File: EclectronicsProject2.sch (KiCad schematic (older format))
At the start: 65 parts, among them J7 Barrel_Jack, U11 TPS62290DRVR, U8 TPS62290DRVR

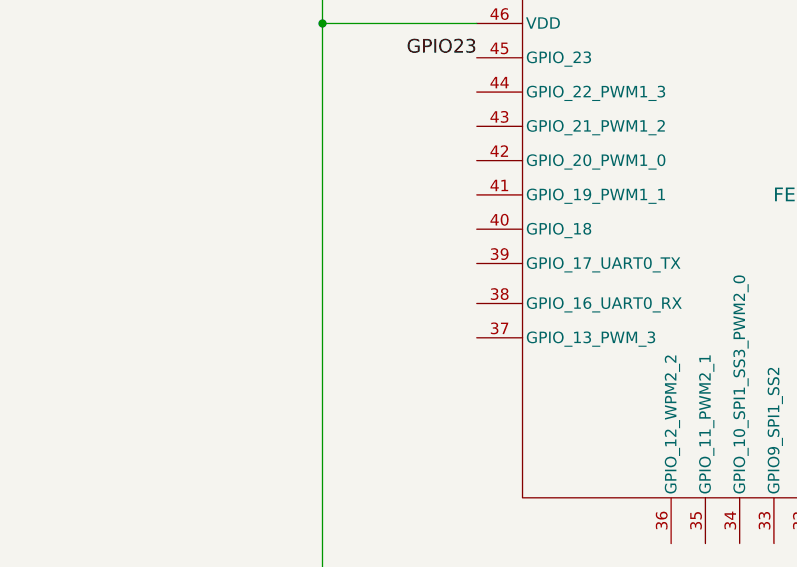
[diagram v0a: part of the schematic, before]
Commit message: adding GPIO UART connections
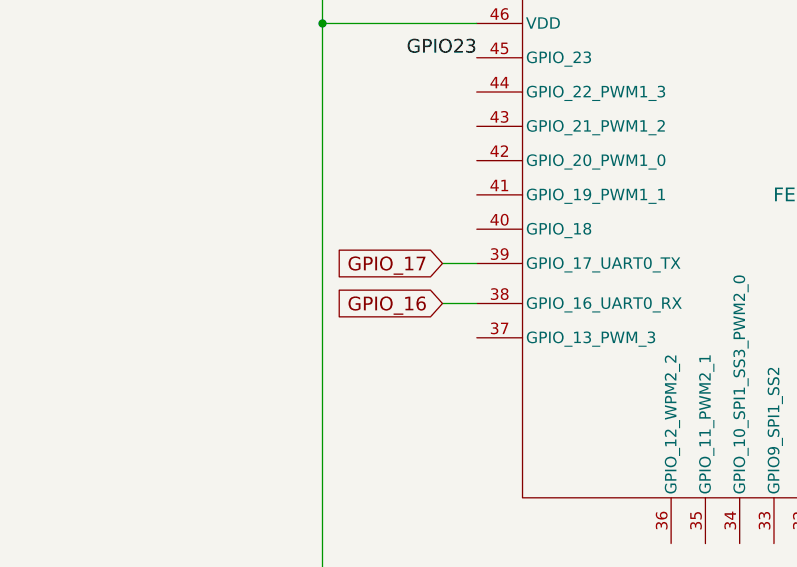
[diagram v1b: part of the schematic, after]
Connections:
- net GPIO_16: now reaches X?.38 (GPIO_16_UART0_RX)
- net GPIO_17: now reaches X?.39 (GPIO_17_UART0_TX)
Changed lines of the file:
@@
 Wire Wire Line
 	15125 5000 14975 5000
+Text GLabel 2275 3425 0    60   Input ~ 0
+GPIO_16
+Text GLabel 2275 3250 0    60   Input ~ 0
+GPIO_17
+Wire Wire Line
+	2275 3250 2425 3250
+Wire Wire Line
+	2275 3425 2425 3425
 $EndSCHEMATC

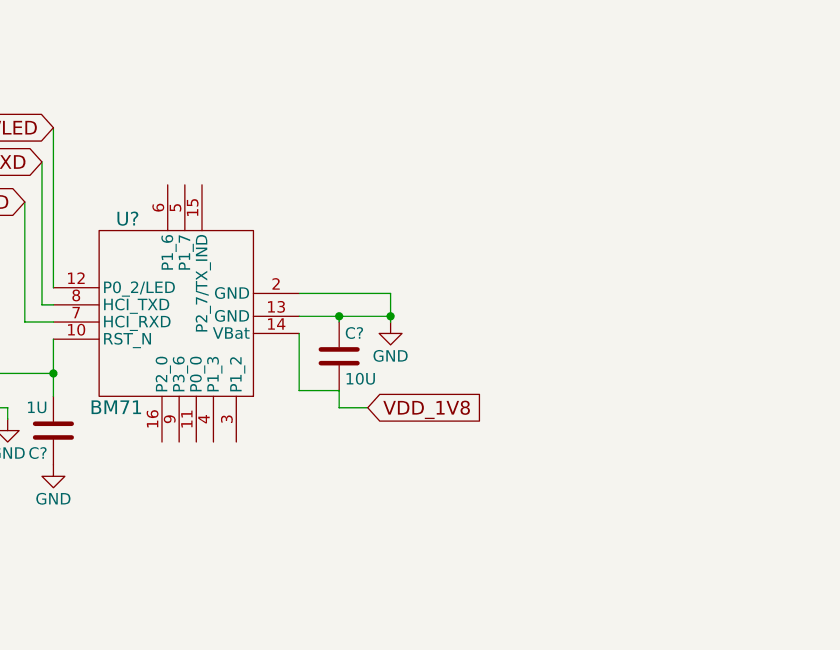
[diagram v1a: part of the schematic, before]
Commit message: added header pins to bm71 bluetooth
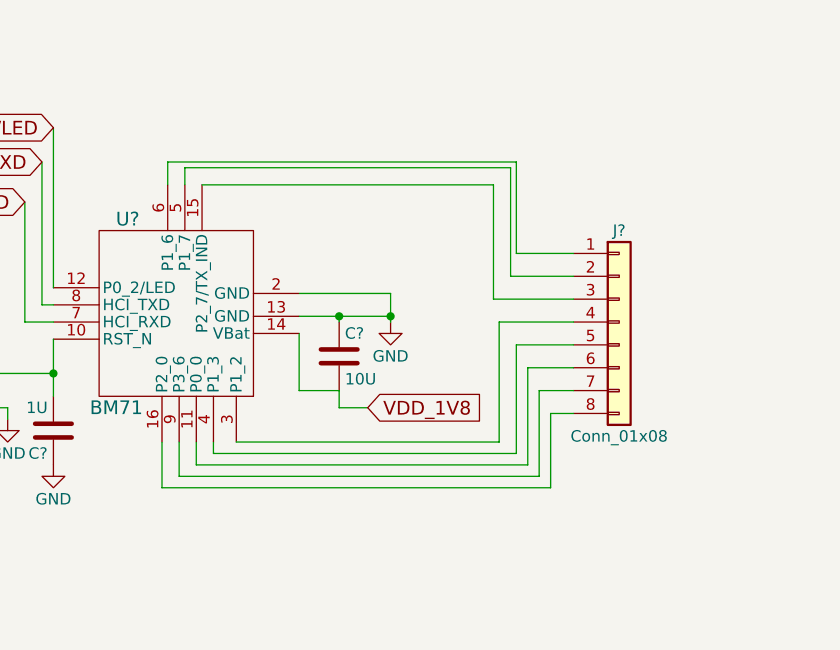
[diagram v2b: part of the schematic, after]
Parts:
- added J?: Conn_01x08, symbol Conn_01x08
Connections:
- net at U?.11 (P0_0): now also J?.6 (Pin_6)
- net at U?.15 (P2_7/TX_IND): now also J?.3 (Pin_3)
- net at U?.16 (P2_0): now also J?.8 (Pin_8)
- net at U?.3 (P1_2): now also J?.4 (Pin_4)
- net at U?.4 (P1_3): now also J?.5 (Pin_5)
- net at U?.5 (P1_7): now also J?.2 (Pin_2)
- net at U?.6 (P1_6): now also J?.1 (Pin_1)
- net at U?.9 (P3_6): now also J?.7 (Pin_7)
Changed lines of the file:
@@
 Wire Wire Line
 	2275 3425 2425 3425
+$Comp
+L Conn_01x08 J?
+U 1 1 59CE5643
+P 4625 6975
+F 0 "J?" H 4625 7375 50  0000 C CNN
+F 1 "Conn_01x08" H 4625 6475 50  0000 C CNN
+F 2 "" H 4625 6975 50  0001 C CNN
+F 3 "" H 4625 6975 50  0001 C CNN
+	1    4625 6975
+	1    0    0    -1
+$EndComp
+Wire Wire Line
+	2650 6375 2650 6275
+Wire Wire Line
+	2650 6275 4175 6275
+Wire Wire Line
+	4175 6275 4175 6675
+Wire Wire Line
+	4175 6675 4425 6675
+Wire Wire Line
+	2725 6375 2725 6300
+Wire Wire Line
+	2725 6300 4150 6300
+Wire Wire Line
+	4150 6300 4150 6775
+Wire Wire Line
+	4150 6775 4425 6775
+Wire Wire Line
+	2800 6375 4075 6375
+Wire Wire Line
+	4075 6375 4075 6875
+Wire Wire Line
+	4075 6875 4425 6875
+Wire Wire Line
+	2950 7500 4100 7500
+Wire Wire Line
+	4100 7500 4100 6975
+Wire Wire Line
+	4100 6975 4425 6975
+Wire Wire Line
+	2850 7500 2850 7550
+Wire Wire Line
+	2850 7550 4175 7550
+Wire Wire Line
+	4175 7550 4175 7075
+Wire Wire Line
+	4175 7075 4425 7075
+Wire Wire Line
+	4225 7175 4425 7175
+Wire Wire Line
+	4225 7175 4225 7600
+Wire Wire Line
+	4225 7600 2775 7600
+Wire Wire Line
+	2775 7600 2775 7500
+Wire Wire Line
+	4425 7275 4275 7275
+Wire Wire Line
+	4275 7275 4275 7650
+Wire Wire Line
+	4275 7650 2700 7650
+Wire Wire Line
+	2700 7650 2700 7500
+Wire Wire Line
+	4425 7375 4325 7375
+Wire Wire Line
+	4325 7375 4325 7700
+Wire Wire Line
+	4325 7700 2625 7700
+Wire Wire Line
+	2625 7700 2625 7500
 $EndSCHEMATC

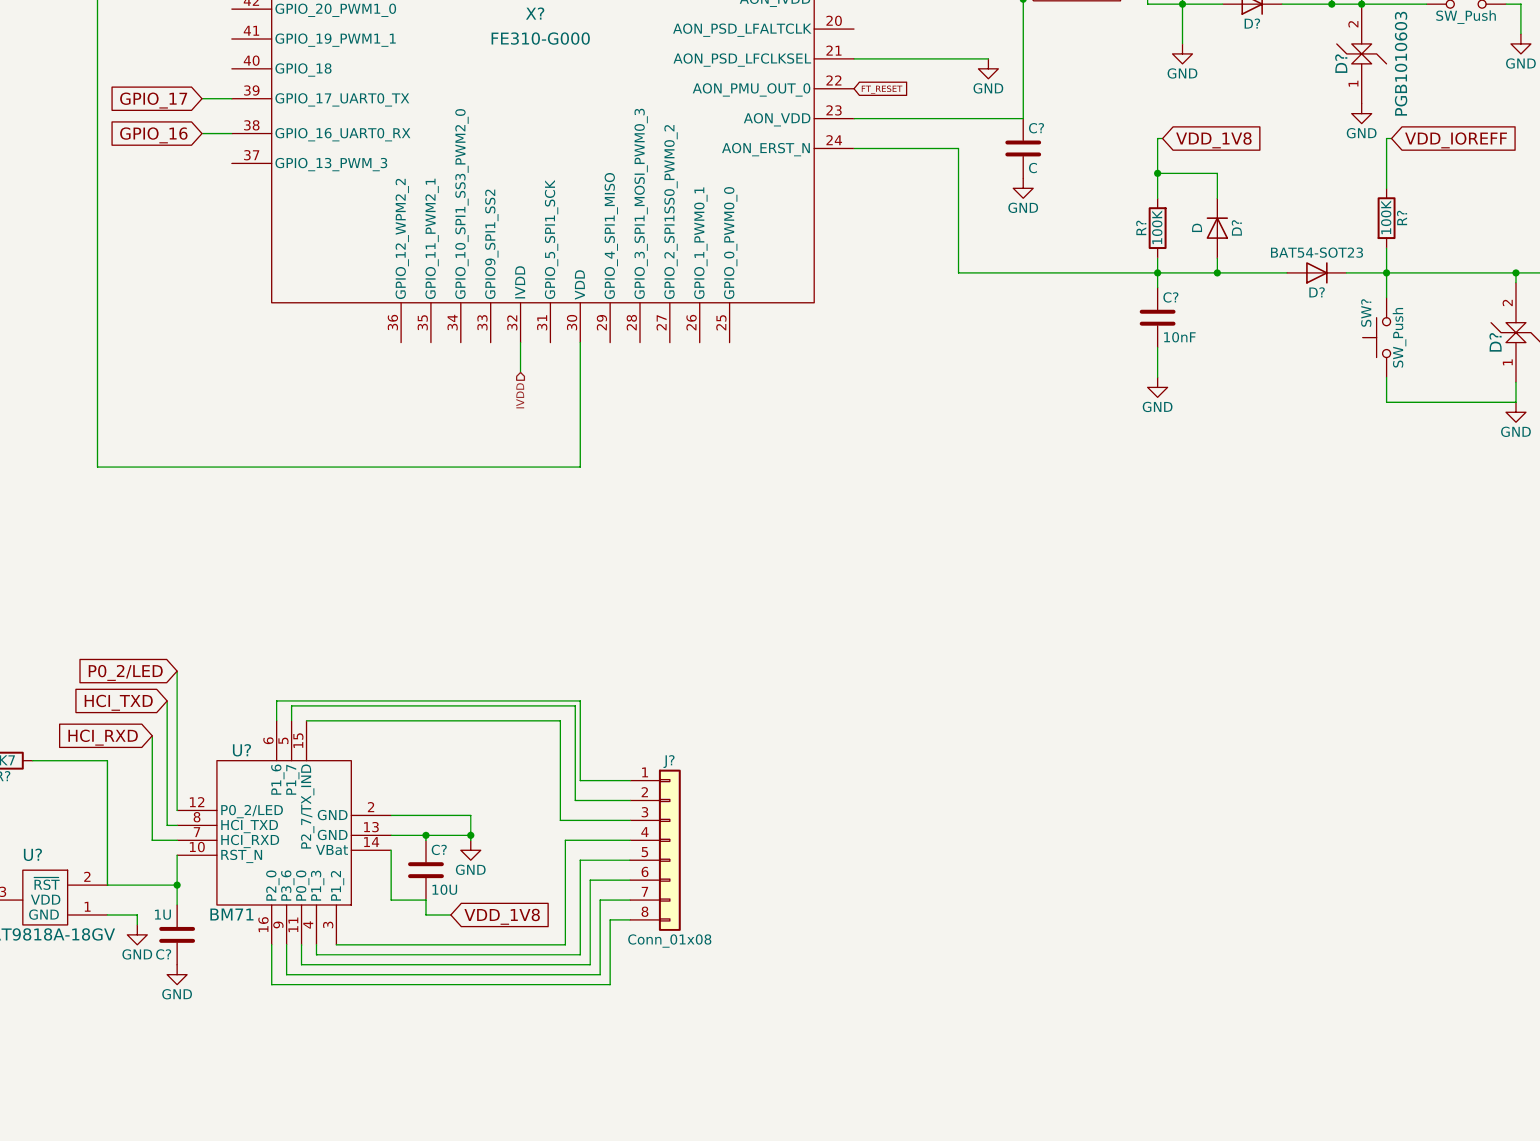
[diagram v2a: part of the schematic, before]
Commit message: attempted to add one of the TXS to header blocks, might be totally wrong
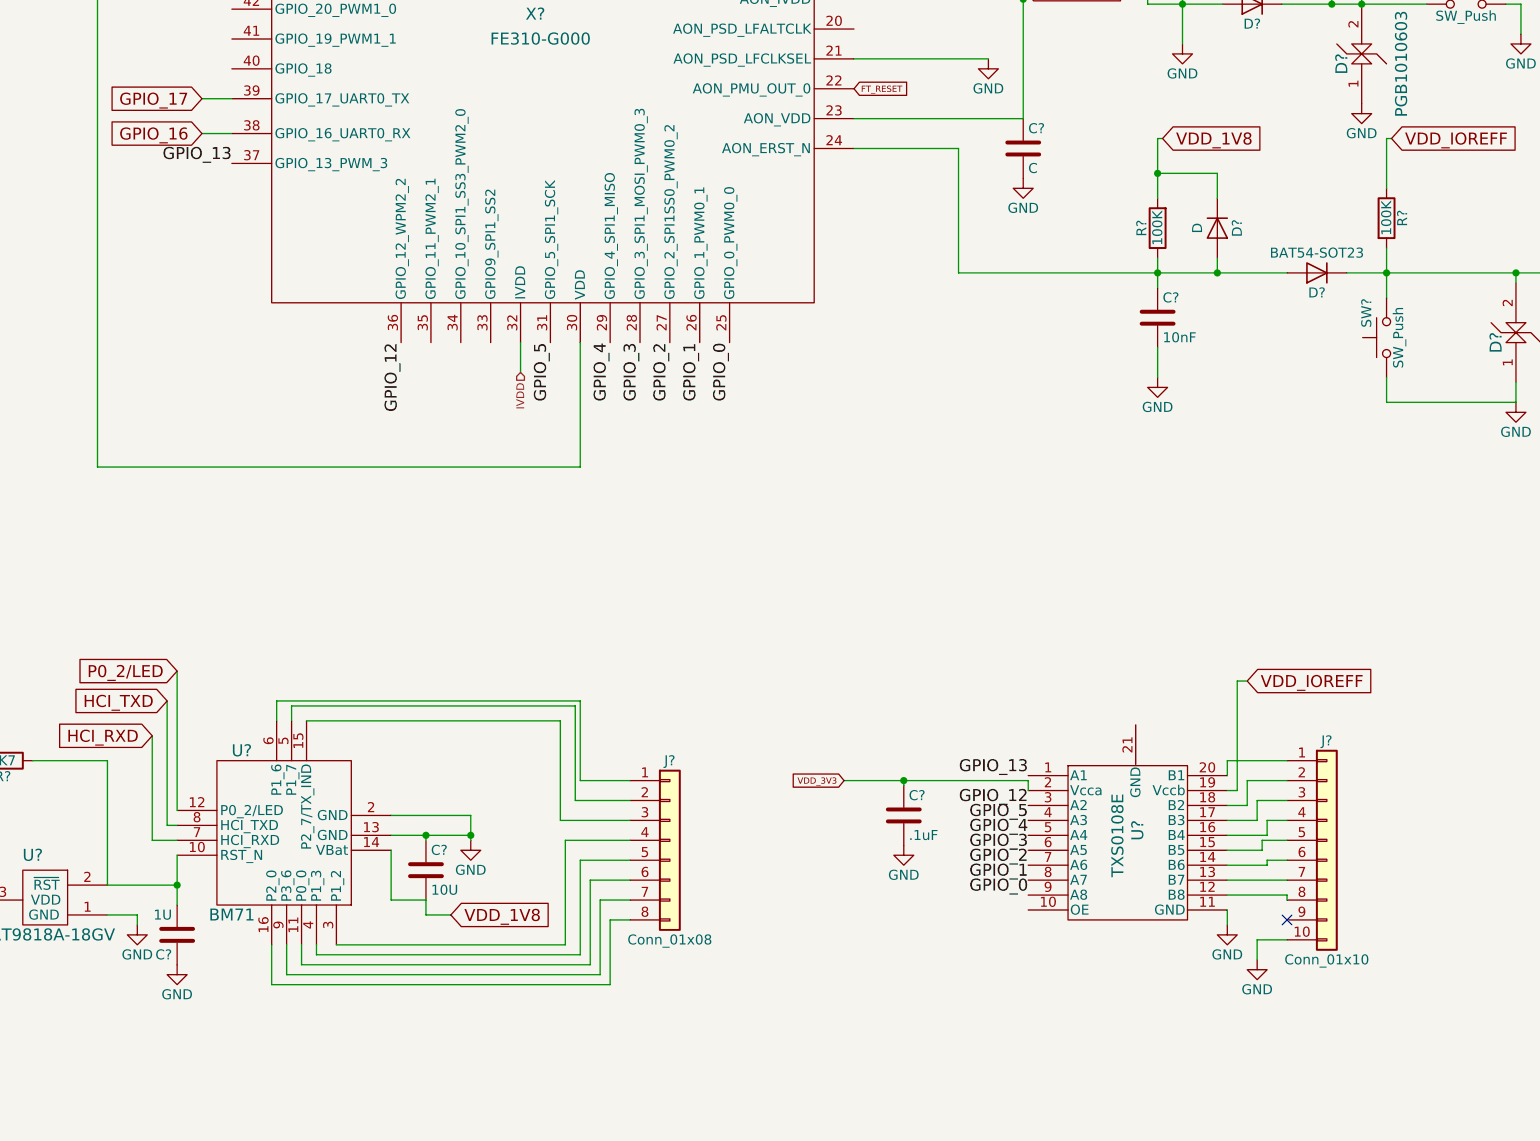
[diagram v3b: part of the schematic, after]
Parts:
- added C?: .1uF, symbol C
- added J?: Conn_01x10, symbol Conn_01x10
- added U?: TXS0108E, symbol TXS0108E
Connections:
- net GND: now also C?.2, J?.10 (Pin_10), U?.11 (GND)
- net VDD_3V3: now also C?.1, U?.2 (Vcca)
- net VDD_IOREFF: now also U?.19 (Vccb)
- net GPIO_0: now reaches X?.25 (GPIO_0_PWM0_0)
- net GPIO_0: now also U?.9 (A8)
- net GPIO_1: now reaches X?.26 (GPIO_1_PWM0_1)
- net GPIO_1: now also U?.8 (A7)
- net GPIO_2: now reaches X?.27 (GPIO_2_SPI1SS0_PWM0_2)
- net GPIO_2: now also U?.7 (A6)
- net GPIO_3: now reaches X?.28 (GPIO_3_SPI1_MOSI_PWM0_3)
- net GPIO_3: now also U?.6 (A5)
- net GPIO_4: now reaches X?.29 (GPIO_4_SPI1_MISO)
- net GPIO_4: now also U?.5 (A4)
- net GPIO_5: now reaches X?.31 (GPIO_5_SPI1_SCK)
- net GPIO_5: now also U?.4 (A3)
- net GPIO_12: now reaches X?.36 (GPIO_12_WPM2_2)
- net GPIO_12: now also U?.3 (A2)
- net GPIO_13: now reaches X?.37 (GPIO_13_PWM_3)
- net GPIO_13: now also U?.1 (A1)
- new net: J?.1 (Pin_1), U?.20 (B1)
- new net: J?.2 (Pin_2), U?.18 (B2)
- new net: J?.3 (Pin_3), U?.17 (B3)
- new net: J?.4 (Pin_4), U?.16 (B4)
- new net: J?.5 (Pin_5), U?.15 (B5)
- new net: J?.6 (Pin_6), U?.14 (B6)
- new net: J?.7 (Pin_7), U?.13 (B7)
- new net: J?.8 (Pin_8), U?.12 (B8)
- no-connect marks 1 -> 2

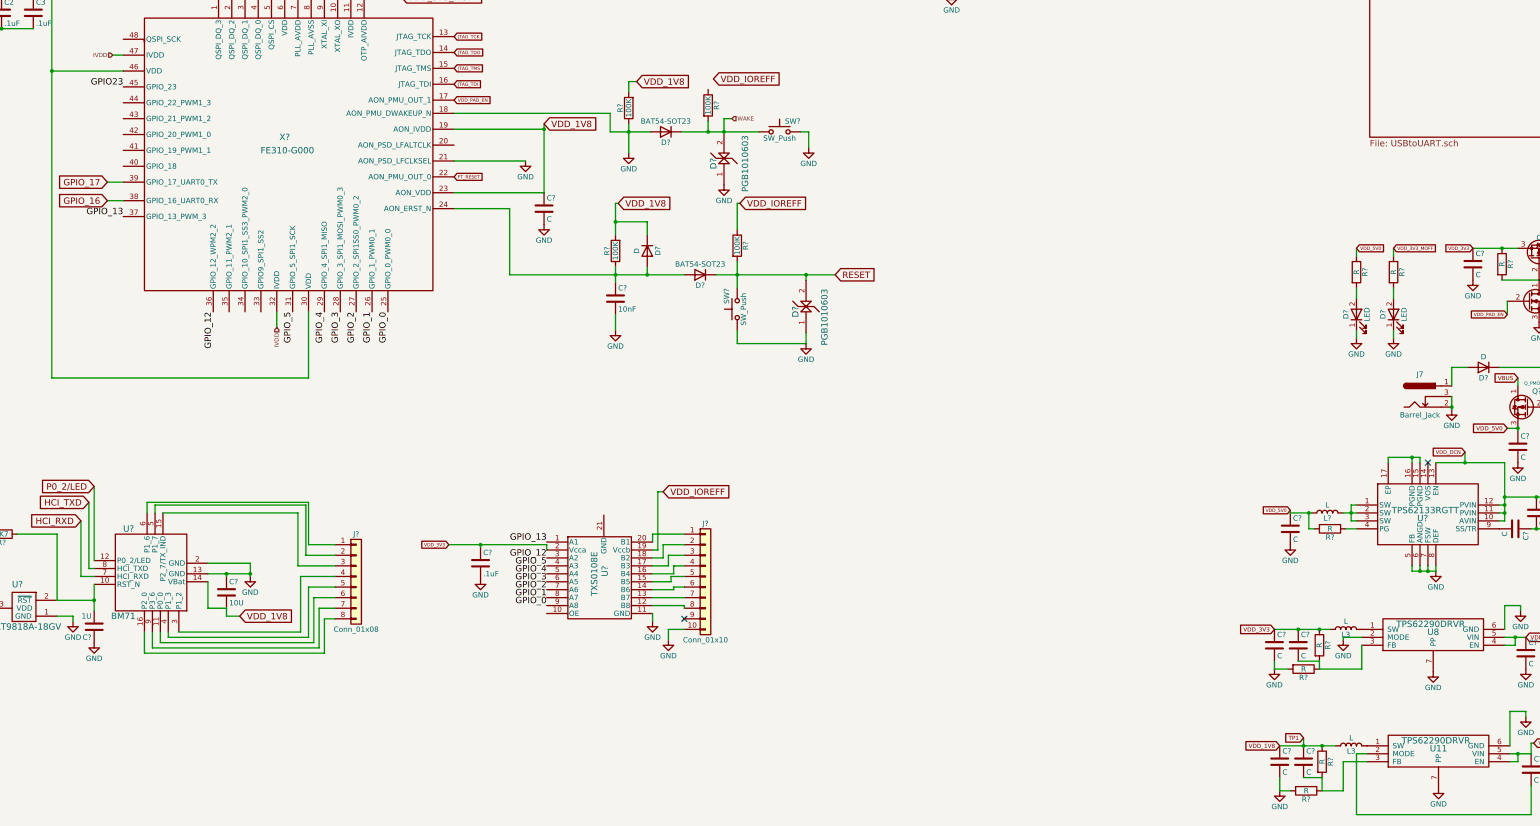
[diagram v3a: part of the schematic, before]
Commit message: added more pinouts
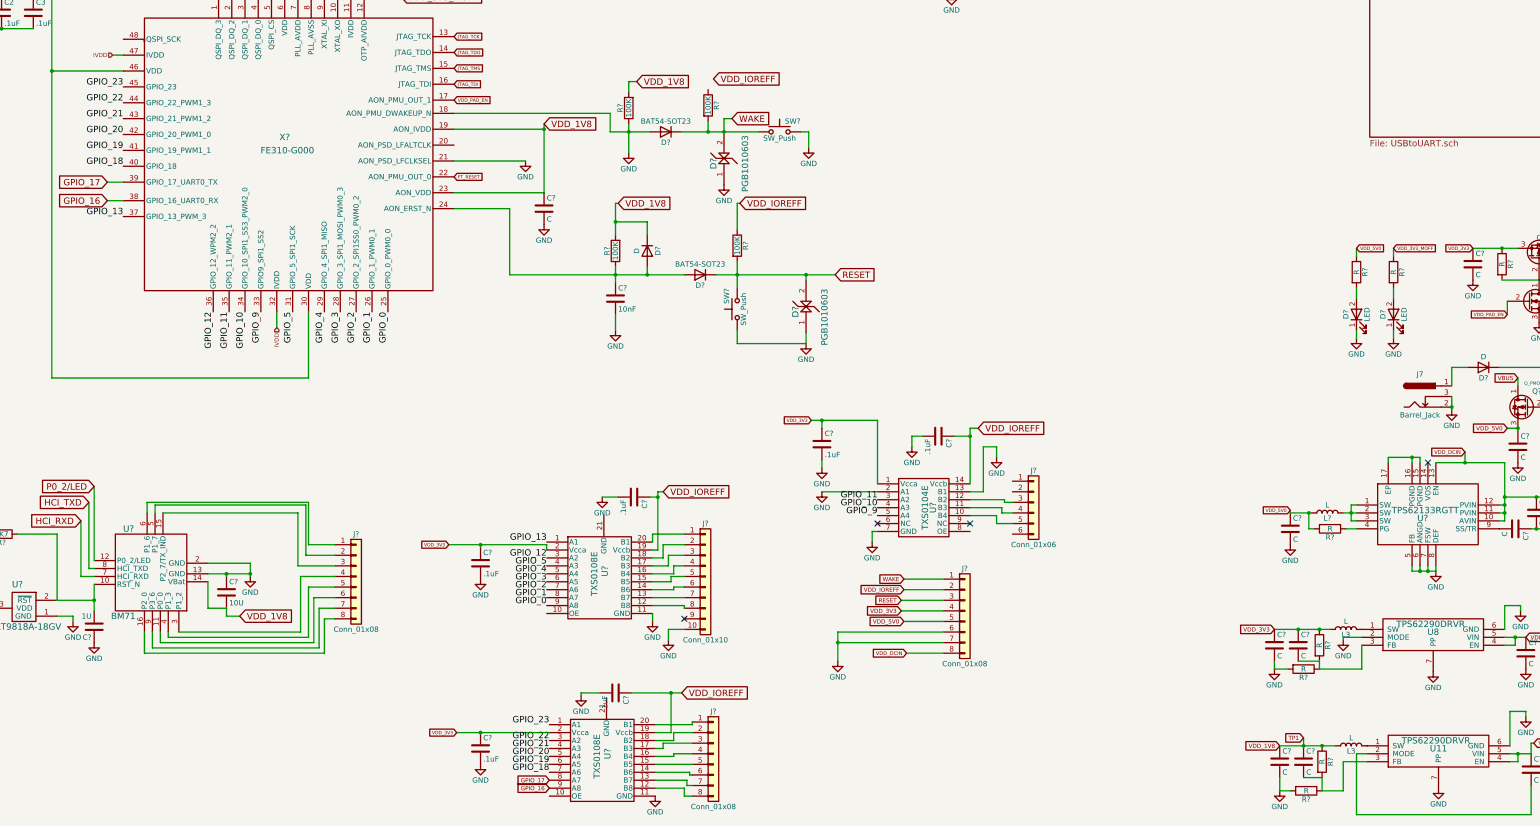
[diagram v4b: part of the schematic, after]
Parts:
- added C? (x5): .1uF, symbol C
- added J?: Conn_01x06, symbol Conn_01x06
- added J? (x2): Conn_01x08, symbol Conn_01x08
- added U?: TXS0104E, symbol TXS0104E
- added U?: TXS0108E, symbol TXS0108E
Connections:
- net GND: now also C?.2, C?.2, C?.2, C?.2, C?.2, J?.6 (Pin_6), J?.7 (Pin_7), U?.11 (GND), U?.13 (B1), U?.2 (A1), U?.7 (GND)
- net GPIO_16: now also U?.9 (A8)
- net GPIO_17: now also U?.8 (A7)
- net RESET: now also J?.3 (Pin_3)
- net VDD_3V3: now also C?.1, C?.1, J?.4 (Pin_4), U?.1 (Vcca), U?.2 (Vcca)
- net VDD_5V0: now also J?.5 (Pin_5)
- net VDD_IOREFF: now also C?.1, C?.1, C?.1, J?.2 (Pin_2), U?.14 (Vccb), U?.19 (Vccb)
- net WAKE: now also J?.1 (Pin_1)
- net GPIO_9: now reaches X?.33 (GPIO9_SPI1_SS2)
- net GPIO_9: now also U?.5 (A4)
- net GPIO_10: now reaches X?.34 (GPIO_10_SPI1_SS3_PWM2_0)
- net GPIO_10: now also U?.4 (A3)
- net GPIO_11: now reaches X?.35 (GPIO_11_PWM2_1)
- net GPIO_11: now also U?.3 (A2)
- net GPIO_18: now reaches X?.40 (GPIO_18)
- net GPIO_18: now also U?.7 (A6)
- net GPIO_19: now reaches X?.41 (GPIO_19_PWM1_1)
- net GPIO_19: now also U?.6 (A5)
- net GPIO_20: now reaches X?.42 (GPIO_20_PWM1_0)
- net GPIO_20: now also U?.5 (A4)
- net GPIO_21: now reaches X?.43 (GPIO_21_PWM1_2)
- net GPIO_21: now also U?.4 (A3)
- net GPIO_22: now reaches X?.44 (GPIO_22_PWM1_3)
- net GPIO_22: now also U?.3 (A2)
- net GPIO23 renamed GPIO_23
- net GPIO_23: now also U?.1 (A1)
- net VDD_DCN renamed VDD_DCIN
- net VDD_DCIN: now also J?.8 (Pin_8)
- new net: J?.5 (Pin_5), U?.10 (B4)
- new net: J?.4 (Pin_4), U?.11 (B3)
- new net: J?.3 (Pin_3), U?.12 (B2)
- new net: J?.8 (Pin_8), U?.12 (B8)
- new net: J?.7 (Pin_7), U?.13 (B7)
- new net: J?.6 (Pin_6), U?.14 (B6)
- new net: J?.5 (Pin_5), U?.15 (B5)
- new net: J?.4 (Pin_4), U?.16 (B4)
- new net: J?.3 (Pin_3), U?.17 (B3)
- new net: J?.2 (Pin_2), U?.18 (B2)
- new net: J?.1 (Pin_1), U?.20 (B1)
- no-connect marks 2 -> 4
